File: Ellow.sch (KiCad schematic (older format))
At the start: 56 parts

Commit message: more updates, not complete
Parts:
- removed D? (x27): 1N4148W, Diode_SMD:D_SOD-123, symbol Diode:1N4148W
- added C?: 10uF, symbol Device:C_Small
- added D?: LED, symbol Device:LED
- added D? (x28): D_Small, symbol Device:D_Small
- added D?: 1N5819, Diode_THT:D_DO-41_SOD81_P10.16mm_Horizontal, symbol Diode:1N5819
- added J?: USB_C_Receptacle_USB2.0, symbol Connector:USB_C_Receptacle_USB2.0
- added Q? (x2): A03407, symbol Device:Q_PMOS_GSD
- added R? (x2): 10k, symbol Device:R_Small
- added R? (x2): 2M, symbol Device:R_Small
- added R?: 820k, symbol Device:R_Small
- added R? (x3): 5.1k, symbol Device:R_Small
- added R?: 100k, symbol Device:R_Small
- added U?: LN2054Y42AMR, symbol ELLOW:LN2054Y42AMR
- added U?: AP2112K-3.3, Package_TO_SOT_SMD:SOT-23-5, symbol Regulator_Linear:AP2112K-3.3
- added Y?: 32.768kHz, symbol Device:Crystal
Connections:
- net labels added: BATTERY_MEASURE, DATA+, DATA-, DCCH, ENCODE_A, ENCODE_B, EXT_VCC, EXT_VCC_CONTROL, GND, PROG, RESET, SWC, SWD, VBAT, VBUS, VDD_H
- wire segments 58 -> 173
- no-connect marks 0 -> 2

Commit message: schematic getting close to ready for pcb start
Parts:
- removed R?: 5.1k, symbol Device:R_Small
- added C?: 4.7uF, symbol Device:C_Small
- added J?: 686116183422, 686116183422, symbol 686116183422:686116183422
- added J?: Conn_01x02_Female, symbol Connector:Conn_01x02_Female
- C?: value 10uF -> 4.7uF
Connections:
- wire segments 173 -> 192
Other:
- moved on the sheet: D?, Q?, R?
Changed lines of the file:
@@
 P 3700 1800
 F 0 "C?" V 3471 1800 50  0000 C CNN
-F 1 "10uF" V 3562 1800 50  0000 C CNN
+F 1 "4.7uF" V 3562 1800 50  0000 C CNN
 F 2 "" H 3700 1800 50  0001 C CNN
 F 3 "~" H 3700 1800 50  0001 C CNN
@@
 $Comp
 L Device:R_Small R?
-U 1 1 5FD9AAA4
-P 5300 900
-F 0 "R?" H 5359 946 50  0000 L CNN
-F 1 "5.1k" H 5359 855 50  0000 L CNN
-F 2 "" H 5300 900 50  0001 C CNN
-F 3 "~" H 5300 900 50  0001 C CNN
-	1    5300 900
-	1    0    0    -1
-$EndComp
-$Comp
-L Device:R_Small R?
 U 1 1 5FDA8766
 P 2200 1600
@@
 L Device:Q_PMOS_GSD Q?
 U 1 1 5FDDABC3
-P -700 3950
-F 0 "Q?" H -495 3996 50  0000 L CNN
-F 1 "A03407" H -495 3905 50  0000 L CNN
-F 2 "" H -500 4050 50  0001 C CNN
-F 3 "~" H -700 3950 50  0001 C CNN
-	1    -700 3950
-	1    0    0    -1
-$EndComp
-Text GLabel -1250 3950 0    50   Input ~ 0
+P -700 3850
+F 0 "Q?" H -495 3896 50  0000 L CNN
+F 1 "A03407" H -495 3805 50  0000 L CNN
+F 2 "" H -500 3950 50  0001 C CNN
+F 3 "~" H -700 3850 50  0001 C CNN
+	1    -700 3850
+	1    0    0    -1
+$EndComp
+Text GLabel -1250 3850 0    50   Input ~ 0
 VBUS
 $Comp
 L Diode:1N5819 D?
 U 1 1 5FDE8A85
-P -1050 4250
-F 0 "D?" H -1050 4033 50  0000 C CNN
-F 1 "1N5819" H -1050 4124 50  0000 C CNN
-F 2 "Diode_THT:D_DO-41_SOD81_P10.16mm_Horizontal" H -1050 4075 50  0001 C CNN
-F 3 "http://www.vishay.com/docs/88525/1n5817.pdf" H -1050 4250 50  0001 C CNN
-	1    -1050 4250
+P -1050 4150
+F 0 "D?" H -1050 3933 50  0000 C CNN
+F 1 "1N5819" H -1050 4024 50  0000 C CNN
+F 2 "Diode_THT:D_DO-41_SOD81_P10.16mm_Horizontal" H -1050 3975 50  0001 C CNN
+F 3 "http://www.vishay.com/docs/88525/1n5817.pdf" H -1050 4150 50  0001 C CNN
+	1    -1050 4150
 	-1   0    0    1
 $EndComp
 Wire Wire Line
-	-1250 3950 -1200 3950
-Wire Wire Line
-	-900 4250 -1200 4250
-Wire Wire Line
-	-1200 3950 -1200 4250
-Connection ~ -1200 3950
-Wire Wire Line
-	-1200 3950 -900 3950
-Connection ~ -1200 4250
-Wire Wire Line
-	-900 4250 -900 3950
-Connection ~ -900 4250
-Connection ~ -900 3950
+	-1250 3850 -1200 3850
+Wire Wire Line
+	-1200 3850 -1200 4150
+Connection ~ -1200 3850
+Wire Wire Line
+	-1200 3850 -900 3850
+Connection ~ -1200 4150
 $Comp
 L Device:R_Small R?
 U 1 1 5FE0E425
-P -1200 4550
-F 0 "R?" H -1141 4596 50  0000 L CNN
-F 1 "100k" H -1141 4505 50  0000 L CNN
-F 2 "" H -1200 4550 50  0001 C CNN
-F 3 "~" H -1200 4550 50  0001 C CNN
-	1    -1200 4550
+P -1200 4450
+F 0 "R?" H -1141 4496 50  0000 L CNN
+F 1 "100k" H -1141 4405 50  0000 L CNN
+F 2 "" H -1200 4450 50  0001 C CNN
+F 3 "~" H -1200 4450 50  0001 C CNN
+	1    -1200 4450
 	1    0    0    -1
 $EndComp
@@
 L power:GND #PWR?
 U 1 1 5FE369DE
-P -1200 4800
-F 0 "#PWR?" H -1200 4550 50  0001 C CNN
-F 1 "GND" H -1195 4627 50  0000 C CNN
-F 2 "" H -1200 4800 50  0001 C CNN
-F 3 "" H -1200 4800 50  0001 C CNN
-	1    -1200 4800
-	1    0    0    -1
-$EndComp
-Wire Wire Line
-	-1200 4650 -1200 4800
-Wire Wire Line
-	-1200 4450 -1200 4250
+P -1200 4700
+F 0 "#PWR?" H -1200 4450 50  0001 C CNN
+F 1 "GND" H -1195 4527 50  0000 C CNN
+F 2 "" H -1200 4700 50  0001 C CNN
+F 3 "" H -1200 4700 50  0001 C CNN
+	1    -1200 4700
+	1    0    0    -1
+$EndComp
+Wire Wire Line
+	-1200 4550 -1200 4700
+Wire Wire Line
+	-1200 4350 -1200 4150
 Text GLabel -600 3550 1    50   Input ~ 0
 VBAT
 Wire Wire Line
-	-600 3550 -600 3750
-Wire Wire Line
 	350  4500 350  4650
 Wire Wire Line
@@
 Wire Wire Line
 	-50  4150 -50  4100
+Wire Wire Line
+	-600 4050 -600 4150
+Connection ~ -600 4150
+Wire Wire Line
+	-600 3550 -600 3650
+$Comp
+L Device:C_Small C?
+U 1 1 5FBDD976
+P -700 4450
+F 0 "C?" V -929 4450 50  0000 C CNN
+F 1 "4.7uF" V -838 4450 50  0000 C CNN
+F 2 "" H -700 4450 50  0001 C CNN
+F 3 "~" H -700 4450 50  0001 C CNN
+	1    -700 4450
+	1    0    0    -1
+$EndComp
+$Comp
+L power:GND #PWR?
+U 1 1 5FBE6A9A
+P -700 4700
+F 0 "#PWR?" H -700 4450 50  0001 C CNN
+F 1 "GND" H -695 4527 50  0000 C CNN
+F 2 "" H -700 4700 50  0001 C CNN
+F 3 "" H -700 4700 50  0001 C CNN
+	1    -700 4700
+	1    0    0    -1
+$EndComp
+Wire Wire Line
+	-700 4550 -700 4700
+Wire Wire Line
+	-700 4350 -700 4150
+Wire Wire Line
+	-700 4150 -600 4150
+Wire Wire Line
+	-900 4150 -700 4150
+Connection ~ -700 4150
+$Comp
+L 686116183422:686116183422 J?
+U 1 1 5FC18475
+P 5050 6850
+F 0 "J?" H 4993 5783 50  0000 C CNN
+F 1 "686116183422" H 4993 5874 50  0000 C CNN
+F 2 "686116183422" H 5050 6850 50  0001 L BNN
+F 3 "" H 5050 6850 50  0001 L BNN
+	1    5050 6850
+	-1   0    0    1
+$EndComp
+Text GLabel 5500 7550 2    50   Input ~ 0
+row4
+Text GLabel 5500 7450 2    50   Input ~ 0
+row3
+Text GLabel 5500 7350 2    50   Input ~ 0
+row2
+Text GLabel 5500 7250 2    50   Input ~ 0
+row1
+Text GLabel 5500 7150 2    50   Input ~ 0
+row0
+Text GLabel 5500 7050 2    50   Input ~ 0
+col5
+Text GLabel 5500 6950 2    50   Input ~ 0
+col4
+Text GLabel 5500 6850 2    50   Input ~ 0
+col3
+Text GLabel 5500 6750 2    50   Input ~ 0
+col2
+Text GLabel 5500 6650 2    50   Input ~ 0
+col1
+Text GLabel 5500 6550 2    50   Input ~ 0
+col0
+Text GLabel 5500 6450 2    50   Input ~ 0
+ENCODE_B
+Text GLabel 5500 6350 2    50   Input ~ 0
+ENCODE_A
+Text GLabel 5500 6050 2    50   Input ~ 0
+GND
+Wire Wire Line
+	5500 6050 5350 6050
+Wire Wire Line
+	5500 6350 5350 6350
+Wire Wire Line
+	5500 6450 5350 6450
+Wire Wire Line
+	5500 6550 5350 6550
+Wire Wire Line
+	5500 6650 5350 6650
+Wire Wire Line
+	5500 6750 5350 6750
+Wire Wire Line
+	5500 6850 5350 6850
+Wire Wire Line
+	5500 6950 5350 6950
+Wire Wire Line
+	5500 7050 5350 7050
+Wire Wire Line
+	5500 7150 5350 7150
+Wire Wire Line
+	5500 7250 5350 7250
+Wire Wire Line
+	5500 7350 5350 7350
+Wire Wire Line
+	5500 7450 5350 7450
+Wire Wire Line
+	5500 7550 5350 7550
+$Comp
+L Connector:Conn_01x02_Female J?
+U 1 1 5FCE772B
+P 6700 6100
+F 0 "J?" H 6728 6076 50  0000 L CNN
+F 1 "Conn_01x02_Female" H 6728 5985 50  0000 L CNN
+F 2 "" H 6700 6100 50  0001 C CNN
+F 3 "~" H 6700 6100 50  0001 C CNN
+	1    6700 6100
+	1    0    0    -1
+$EndComp
+Text GLabel 6400 6100 0    50   Input ~ 0
+VBAT
+Text GLabel 6400 6200 0    50   Input ~ 0
+GND
+Wire Wire Line
+	6500 6200 6400 6200
+Wire Wire Line
+	6500 6100 6400 6100
 $EndSCHEMATC

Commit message: first parts associated with footprints on pcb
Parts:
- C1, C2: renamed from C?; footprint (none) -> Capacitor_SMD:C_0603_1608Metric_Pad1.08x0.95mm_HandSolder
- D10, D11, D12, D13, D14, D15, D16, D17, D18, D19, D20, D21, D22, D23, D24, D25, D26, D27, D28, D29, D3, D30, D4, D5, D6, D7, D8, D9: renamed from D?; footprint (none) -> Diode_SMD:D_SOD-123
- D2: renamed from D?; footprint (none) -> LED_SMD:LED_0603_1608Metric
- J2: renamed from J?; footprint 686116183422 -> 686116183422:686116183422
- J3: renamed from J?; footprint (none) -> Connector_PinHeader_2.54mm:PinHeader_1x02_P2.54mm_Vertical
- Q1, Q2: renamed from Q?; footprint (none) -> Package_TO_SOT_SMD:SOT-23_Handsoldering
- R1, R2, R3, R4, R5, R6, R7, R8: renamed from R?; footprint (none) -> Resistor_SMD:R_0603_1608Metric_Pad0.98x0.95mm_HandSolder
- SW9: renamed from SW?; footprint (none) -> Rotary_Encoder:RotaryEncoder_Alps_EC11E-Switch_Vertical_H20mm
- gave numbers to parts that had none: 33

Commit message: moved shield stuff to another board
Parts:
- removed D10, D11, D12, D13, D14, D15, D16, D17, D18, D19, D20, D21, D22, D23, D24, D25, D26, D27, D28, D29, D3, D30, D4, D5, D6, D7, D8, D9: D_Small, Diode_SMD:D_SOD-123, symbol Device:D_Small
- removed J2: 686116183422, 686116183422:686116183422, symbol 686116183422:686116183422
- removed SW1, SW10, SW11, SW12, SW13, SW14, SW15, SW16, SW17, SW18, SW19, SW2, SW20, SW21, SW22, SW23, SW24, SW25, SW26, SW27, SW28, SW3, SW4, SW5, SW6, SW7, SW8: SW_SPST, symbol Switch:SW_SPST
- removed SW9: RotaryEncoder_Switch, Rotary_Encoder:RotaryEncoder_Alps_EC11E-Switch_Vertical_H20mm, symbol Device:RotaryEncoder_Switch
- added J4: Bus_M.2_Socket_A, ellow:M_2_EdgeConnector, symbol Connector:Bus_M.2_Socket_A
- J1: footprint (none) -> Connector_USB:USB_C_Receptacle_HRO_TYPE-C-31-M-12
- U2: footprint (none) -> ellow:E73-2G4M08S1C-52840
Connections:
- net labels removed: ENCODE_A, ENCODE_B, col0, col1, col2, col3, col4, col5, row0, row1, row2, row3, row4
- wire segments 192 -> 89

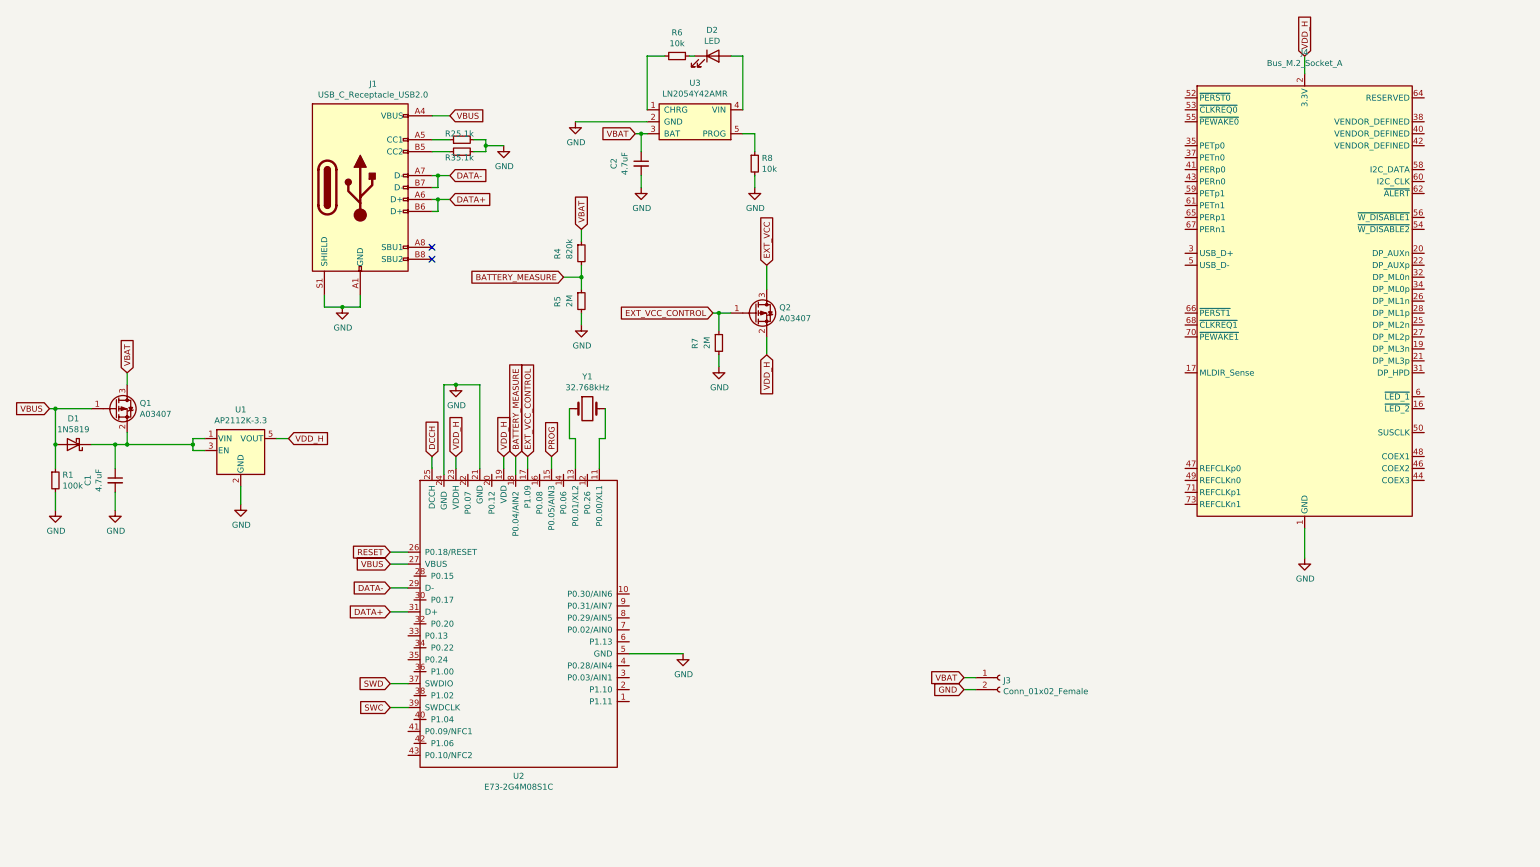
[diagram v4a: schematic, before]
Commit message: first board for quote check. not routed
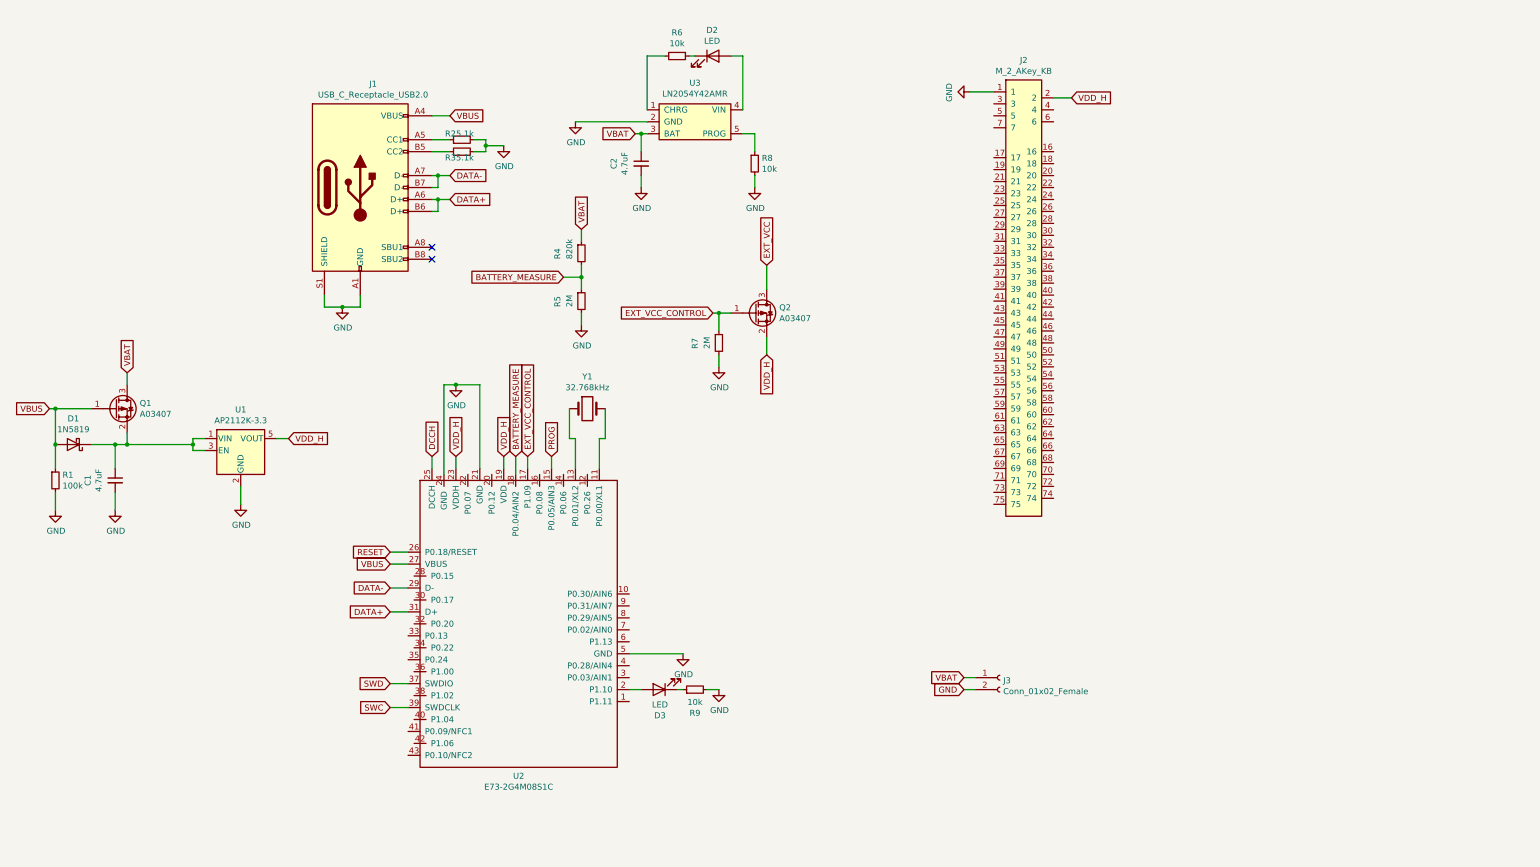
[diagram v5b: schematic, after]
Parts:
- removed J4: Bus_M.2_Socket_A, ellow:M_2_EdgeConnector, symbol Connector:Bus_M.2_Socket_A
- added D3: LED, LED_SMD:LED_0603_1608Metric, symbol Device:LED
- added J2: M_2_AKey_KB, ellow:M_2_EdgeConnector_A_Key, symbol ELLOW:M_2_AKey_KB
- added R9: 10k, Resistor_SMD:R_0603_1608Metric_Pad0.98x0.95mm_HandSolder, symbol Device:R_Small
- D1: footprint Diode_THT:D_DO-41_SOD81_P10.16mm_Horizontal -> Diode_SMD:D_SOD-323_HandSoldering
- U3: footprint (none) -> Package_TO_SOT_SMD:SOT-23-5_HandSoldering
- Y1: footprint (none) -> Crystal:Crystal_SMD_2012-2Pin_2.0x1.2mm_HandSoldering
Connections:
- net GND: now also J2.1, R9.2
- net VDD_H: now also J2.2
- net at U2.2 (P1.10): now also D3.2 (A)
- new net: D3.1 (K), R9.1
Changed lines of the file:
@@
 F 0 "Y1" H 3250 4118 50  0000 C CNN
 F 1 "32.768kHz" H 3250 4027 50  0000 C CNN
-F 2 "" H 3250 3850 50  0001 C CNN
+F 2 "Crystal:Crystal_SMD_2012-2Pin_2.0x1.2mm_HandSoldering" H 3250 3850 50  0001 C CNN
 F 3 "~" H 3250 3850 50  0001 C CNN
 	1    3250 3850
@@
 F 0 "U3" H 4150 1775 50  0000 C CNN
 F 1 "LN2054Y42AMR" H 4150 1684 50  0000 C CNN
-F 2 "" H 3950 1500 50  0001 C CNN
+F 2 "Package_TO_SOT_SMD:SOT-23-5_HandSoldering" H 3950 1500 50  0001 C CNN
 F 3 "" H 3950 1500 50  0001 C CNN
 	1    4150 1450
@@
 F 0 "D1" H -1050 3933 50  0000 C CNN
 F 1 "1N5819" H -1050 4024 50  0000 C CNN
-F 2 "Diode_THT:D_DO-41_SOD81_P10.16mm_Horizontal" H -1050 3975 50  0001 C CNN
+F 2 "Diode_SMD:D_SOD-323_HandSoldering" H -1050 3975 50  0001 C CNN
 F 3 "http://www.vishay.com/docs/88525/1n5817.pdf" H -1050 4150 50  0001 C CNN
 	1    -1050 4150
@@
 Wire Wire Line
 	6500 6100 6400 6100
-$Comp
-L Connector:Bus_M.2_Socket_A J4
-U 1 1 5FBB0B59
-P 9250 2950
-F 0 "J4" H 9250 5031 50  0000 C CNN
-F 1 "Bus_M.2_Socket_A" H 9250 4940 50  0000 C CNN
-F 2 "ellow:M_2_EdgeConnector" H 9250 4000 50  0001 C CNN
-F 3 "http://read.pudn.com/downloads794/doc/project/3133918/PCIe_M.2_Electromechanical_Spec_Rev1.0_Final_11012013_RS_Clean.pdf#page=148" H 9250 4000 50  0001 C CNN
-	1    9250 2950
-	1    0    0    -1
-$EndComp
-Text GLabel 9250 900  1    50   Input ~ 0
+Text GLabel 7300 1250 2    50   Input ~ 0
 VDD_H
-Wire Wire Line
-	9250 1050 9250 900
-$Comp
-L power:GND #PWR?
+$Comp
+L power:GND #PWR0104
 U 1 1 5FBE92AA
-P 9250 5100
-F 0 "#PWR?" H 9250 4850 50  0001 C CNN
-F 1 "GND" H 9255 4927 50  0000 C CNN
-F 2 "" H 9250 5100 50  0001 C CNN
-F 3 "" H 9250 5100 50  0001 C CNN
-	1    9250 5100
-	1    0    0    -1
-$EndComp
-Wire Wire Line
-	9250 4850 9250 5100
+P 6450 1200
+F 0 "#PWR0104" H 6450 950 50  0001 C CNN
+F 1 "GND" H 6455 1027 50  0000 C CNN
+F 2 "" H 6450 1200 50  0001 C CNN
+F 3 "" H 6450 1200 50  0001 C CNN
+	1    6450 1200
+	0    1    1    0
+$EndComp
+$Comp
+L ELLOW:M_2_AKey_KB J2
+U 1 1 5FC057BA
+P 6850 1000
+F 0 "J2" H 6900 1065 50  0000 C CNN
+F 1 "M_2_AKey_KB" H 6900 974 50  0000 C CNN
+F 2 "ellow:M_2_EdgeConnector_A_Key" H 6850 1000 50  0001 C CNN
+F 3 "" H 6850 1000 50  0001 C CNN
+	1    6850 1000
+	1    0    0    -1
+$EndComp
+Wire Wire Line
+	7300 1250 7150 1250
+Wire Wire Line
+	6650 1200 6450 1200
+$Comp
+L Device:LED D3
+U 1 1 5FC73EC6
+P 3850 6200
+F 0 "D3" H 3843 6417 50  0000 C CNN
+F 1 "LED" H 3843 6326 50  0000 C CNN
+F 2 "LED_SMD:LED_0603_1608Metric" H 3850 6200 50  0001 C CNN
+F 3 "~" H 3850 6200 50  0001 C CNN
+	1    3850 6200
+	-1   0    0    1
+$EndComp
+$Comp
+L Device:R_Small R9
+U 1 1 5FC73ECC
+P 4150 6200
+F 0 "R9" V 3954 6200 50  0000 C CNN
+F 1 "10k" V 4045 6200 50  0000 C CNN
+F 2 "Resistor_SMD:R_0603_1608Metric_Pad0.98x0.95mm_HandSolder" H 4150 6200 50  0001 C CNN
+F 3 "~" H 4150 6200 50  0001 C CNN
+	1    4150 6200
+	0    -1   -1   0
+$EndComp
+Wire Wire Line
+	4000 6200 4050 6200
+Wire Wire Line
+	3600 6200 3700 6200
+$Comp
+L power:GND #PWR0114
+U 1 1 5FC76B15
+P 4350 6200
+F 0 "#PWR0114" H 4350 5950 50  0001 C CNN
+F 1 "GND" H 4355 6027 50  0000 C CNN
+F 2 "" H 4350 6200 50  0001 C CNN
+F 3 "" H 4350 6200 50  0001 C CNN
+	1    4350 6200
+	1    0    0    -1
+$EndComp
+Wire Wire Line
+	4250 6200 4350 6200
 $EndSCHEMATC

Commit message: starting to look at routing
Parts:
- added H1: MountingHole, ellow:MountingHole_M.2_3mm, symbol Mechanical:MountingHole
- C1, C2: footprint Capacitor_SMD:C_0603_1608Metric_Pad1.08x0.95mm_HandSolder -> Capacitor_SMD:C_0603_1608Metric
- D1: footprint Diode_SMD:D_SOD-323_HandSoldering -> Diode_SMD:D_SOD-323
- J3: footprint Connector_PinHeader_2.54mm:PinHeader_1x02_P2.54mm_Vertical -> Connector_PinHeader_1.27mm:PinHeader_1x02_P1.27mm_Vertical
- Q1, Q2: footprint Package_TO_SOT_SMD:SOT-23_Handsoldering -> Package_TO_SOT_SMD:SOT-23
- U3: footprint Package_TO_SOT_SMD:SOT-23-5_HandSoldering -> Package_TO_SOT_SMD:SOT-23-5
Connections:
- net DATA+: now also J2.66
- net DATA-: now also J2.67
- net EXT_VCC: now also J2.2
- net GND: now also J2.25, J2.40, J2.53, J2.71
- net RESET: now also J2.6
- net SWC: now also J2.74
- net SWD: now also J2.70
- net VBAT: now also J2.5
- net VDD_H: now also J2.75; no longer J2.2
- net P1.11: now reaches U2.1 (P1.11)
- net P1.11: now also J2.32
- net P0.30: now reaches U2.10 (P0.30/AIN6)
- net P0.30: now also J2.17
- net P0.26: now reaches U2.12 (P0.26)
- net P0.06: now reaches U2.14 (P0.06)
- net P0.08: now reaches U2.16 (P0.08)
- net P0.08: now also J2.52
- net P0.12: now reaches U2.20 (P0.12)
- net 90.07: now reaches U2.22 (P0.07)
- net P0.15: now reaches U2.28 (P0.15)
- net P0.15: now also J2.49
- net P0.03: now reaches U2.3 (P0.03/AIN1)
- net P0.03: now also J2.28
- net P0.17: now reaches U2.30 (P0.17)
- net P0.17: now also J2.48
- net P0.20: now reaches U2.32 (P0.20)
- net P0.20: now also J2.45
- net P0.13: now reaches U2.33 (P0.13)
- net P0.13: now also J2.44
- net P0.22: now reaches U2.34 (P0.22)
- net P0.24: now reaches U2.35 (P0.24)
- net P0.24: now also J2.41
- net P1.00: now reaches U2.36 (P1.00)
- net P1.02: now reaches U2.38 (P1.02)
- net P0.28: now reaches U2.4 (P0.28/AIN4)
- net P0.28: now also J2.29
- net P1.04: now reaches U2.40 (P1.04)
- net P0.09: now reaches U2.41 (P0.09/NFC1)
- net P0.09: now also J2.37
- net P1.06: now reaches U2.42 (P1.06)
- net P1.06: now also J2.33
- net P0.10: now reaches U2.43 (P0.10/NFC2)
- net P0.10: now also J2.36
- net P1.13: now reaches U2.6 (P1.13)
- net P1.13: now also J2.24
- net P0.02: now reaches U2.7 (P0.02/AIN0)
- net P0.02: now also J2.21
- net P0.29: now reaches U2.8 (P0.29/AIN5)
- net P0.29: now also J2.20
- net P0.31: now reaches U2.9 (P0.31/AIN7)
- net P0.31: now also J2.16
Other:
- note added: "Battery Connection"
- note added: "Power & Filtering"
- moved on the sheet: C1, D1, D3, J3, Q1, R1, R9, U1
